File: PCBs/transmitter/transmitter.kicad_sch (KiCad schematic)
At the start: 20 parts, among them J1 Conn_01x02, J11 LoRa, J2 GPIO, J3 Ethernet, J4 Thermistor (10K), J5 RF24, J6 SWD, J7 I2C, J8 Serial, SW1 ~{RESET}

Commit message: created fabrication outputs
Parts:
- H1: footprint (none) -> MountingHole:MountingHole_2mm
- J11, J3: footprint Connector_PinSocket_2.54mm:PinSocket_1x08_P2.54mm_Vertical -> Connector_PinHeader_2.54mm:PinHeader_1x08_P2.54mm_Vertical
- J2, J6, J7, J8: footprint Connector_PinSocket_2.54mm:PinSocket_1x04_P2.54mm_Vertical -> Connector_PinHeader_2.54mm:PinHeader_1x04_P2.54mm_Vertical
- J5: footprint Connector_PinSocket_2.54mm:PinSocket_1x07_P2.54mm_Vertical -> Connector_PinHeader_2.54mm:PinHeader_1x07_P2.54mm_Vertical
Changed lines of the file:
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@@
     (property "Reference" "J11" (id 0) (at 254 92.71 0))
     (property "Value" "LoRa" (id 1) (at 254 95.25 0))
-    (property "Footprint" "Connector_PinSocket_2.54mm:PinSocket_1x08_P2.54mm_Vertical" (id 2) (at 254 109.22 0)
+    (property "Footprint" "Connector_PinHeader_2.54mm:PinHeader_1x08_P2.54mm_Vertical" (id 2) (at 254 109.22 0)
       (effects (font (size 1.27 1.27)) hide)
     )
@@
     (property "Reference" "J3" (id 0) (at 207.01 31.75 0))
     (property "Value" "Ethernet" (id 1) (at 207.01 34.29 0))
-    (property "Footprint" "Connector_PinSocket_2.54mm:PinSocket_1x08_P2.54mm_Vertical" (id 2) (at 207.01 48.26 0)
+    (property "Footprint" "Connector_PinHeader_2.54mm:PinHeader_1x08_P2.54mm_Vertical" (id 2) (at 207.01 48.26 0)
       (effects (font (size 1.27 1.27)) hide)
     )
@@
     (property "Reference" "J5" (id 0) (at 231.14 36.83 0))
     (property "Value" "RF24" (id 1) (at 231.14 39.37 0))
-    (property "Footprint" "Connector_PinSocket_2.54mm:PinSocket_1x07_P2.54mm_Vertical" (id 2) (at 231.14 50.8 0)
+    (property "Footprint" "Connector_PinHeader_2.54mm:PinHeader_1x07_P2.54mm_Vertical" (id 2) (at 231.14 50.8 0)
       (effects (font (size 1.27 1.27)) hide)
     )
@@
     (property "Reference" "J7" (id 0) (at 256.54 40.64 0))
     (property "Value" "I2C" (id 1) (at 256.54 43.18 0))
-    (property "Footprint" "Connector_PinSocket_2.54mm:PinSocket_1x04_P2.54mm_Vertical" (id 2) (at 256.54 52.07 0)
+    (property "Footprint" "Connector_PinHeader_2.54mm:PinHeader_1x04_P2.54mm_Vertical" (id 2) (at 256.54 52.07 0)
       (effects (font (size 1.27 1.27)) hide)
     )
@@
     (property "Reference" "J8" (id 0) (at 257.81 67.31 0))
     (property "Value" "Serial" (id 1) (at 257.81 69.85 0))
-    (property "Footprint" "Connector_PinSocket_2.54mm:PinSocket_1x04_P2.54mm_Vertical" (id 2) (at 257.81 78.74 0)
+    (property "Footprint" "Connector_PinHeader_2.54mm:PinHeader_1x04_P2.54mm_Vertical" (id 2) (at 257.81 78.74 0)
       (effects (font (size 1.27 1.27)) hide)
     )
@@
     (property "Reference" "J6" (id 0) (at 234.95 67.31 0))
     (property "Value" "SWD" (id 1) (at 234.95 69.85 0))
-    (property "Footprint" "Connector_PinSocket_2.54mm:PinSocket_1x04_P2.54mm_Vertical" (id 2) (at 234.95 78.74 0)
+    (property "Footprint" "Connector_PinHeader_2.54mm:PinHeader_1x04_P2.54mm_Vertical" (id 2) (at 234.95 78.74 0)
       (effects (font (size 1.27 1.27)) hide)
     )
@@
     (property "Reference" "J2" (id 0) (at 190.5 62.23 0))
     (property "Value" "GPIO" (id 1) (at 190.5 64.77 0))
-    (property "Footprint" "Connector_PinSocket_2.54mm:PinSocket_1x04_P2.54mm_Vertical" (id 2) (at 190.5 73.66 0)
+    (property "Footprint" "Connector_PinHeader_2.54mm:PinHeader_1x04_P2.54mm_Vertical" (id 2) (at 190.5 73.66 0)
       (effects (font (size 1.27 1.27)) hide)
     )
@@
       (effects (font (size 1.27 1.27)) (justify left))
     )
-    (property "Footprint" "" (id 2) (at 35.56 179.07 0)
+    (property "Footprint" "MountingHole:MountingHole_2mm" (id 2) (at 35.56 179.07 0)
       (effects (font (size 1.27 1.27)) hide)
     )
@@
     )
     (path "/b6492f65-6790-4444-8f40-ae63444e55da"
-      (reference "J2") (unit 1) (value "GPIO") (footprint "Connector_PinSocket_2.54mm:PinSocket_1x04_P2.54mm_Vertical")
+      (reference "J2") (unit 1) (value "GPIO") (footprint "Connector_PinHeader_2.54mm:PinHeader_1x04_P2.54mm_Vertical")
     )
     (path "/148e4b07-2754-41fa-b362-f32ae5e0b598"
-      (reference "J3") (unit 1) (value "Ethernet") (footprint "Connector_PinSocket_2.54mm:PinSocket_1x08_P2.54mm_Vertical")
+      (reference "J3") (unit 1) (value "Ethernet") (footprint "Connector_PinHeader_2.54mm:PinHeader_1x08_P2.54mm_Vertical")
     )
     (path "/fd4589a9-f46c-4fce-a160-6787f4809f25"
@@
     )
     (path "/23618512-a2f8-44e6-8cd2-358294831b6f"
-      (reference "J5") (unit 1) (value "RF24") (footprint "Connector_PinSocket_2.54mm:PinSocket_1x07_P2.54mm_Vertical")
+      (reference "J5") (unit 1) (value "RF24") (footprint "Connector_PinHeader_2.54mm:PinHeader_1x07_P2.54mm_Vertical")
     )
     (path "/9c0e092b-e2d2-4772-898a-4fdfc0c9fe18"
-      (reference "J6") (unit 1) (value "SWD") (footprint "Connector_PinSocket_2.54mm:PinSocket_1x04_P2.54mm_Vertical")
+      (reference "J6") (unit 1) (value "SWD") (footprint "Connector_PinHeader_2.54mm:PinHeader_1x04_P2.54mm_Vertical")
     )
     (path "/3d3b00a9-2614-4561-9134-a45b0c6831cd"
-      (reference "J7") (unit 1) (value "I2C") (footprint "Connector_PinSocket_2.54mm:PinSocket_1x04_P2.54mm_Vertical")
+      (reference "J7") (unit 1) (value "I2C") (footprint "Connector_PinHeader_2.54mm:PinHeader_1x04_P2.54mm_Vertical")
     )
     (path "/4caa9778-cadd-482a-8556-4989310bc954"
-      (reference "J8") (unit 1) (value "Serial") (footprint "Connector_PinSocket_2.54mm:PinSocket_1x04_P2.54mm_Vertical")
+      (reference "J8") (unit 1) (value "Serial") (footprint "Connector_PinHeader_2.54mm:PinHeader_1x04_P2.54mm_Vertical")
     )
     (path "/d7224ebd-0e44-4d03-8a13-9628956cf16f/199f531d-1d56-48d3-bbb1-c98ffceed090"
@@
     )
     (path "/0e660b53-fd61-484a-b5ba-116ad7753a8a"
-      (reference "J11") (unit 1) (value "LoRa") (footprint "Connector_PinSocket_2.54mm:PinSocket_1x08_P2.54mm_Vertical")
+      (reference "J11") (unit 1) (value "LoRa") (footprint "Connector_PinHeader_2.54mm:PinHeader_1x08_P2.54mm_Vertical")
     )
     (path "/165f464f-66cd-43f3-872c-58af3ebdb812/198b5ba2-3238-4b90-8afe-766f8c4b230b"

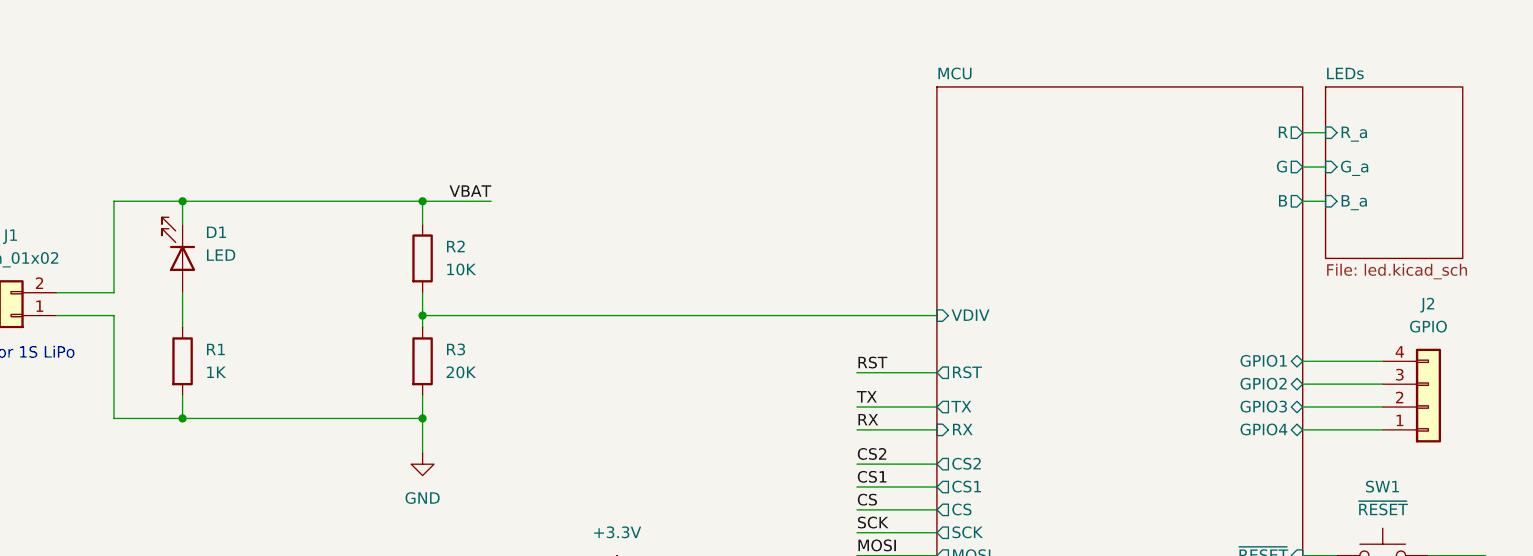
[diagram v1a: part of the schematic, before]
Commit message: created sensor board
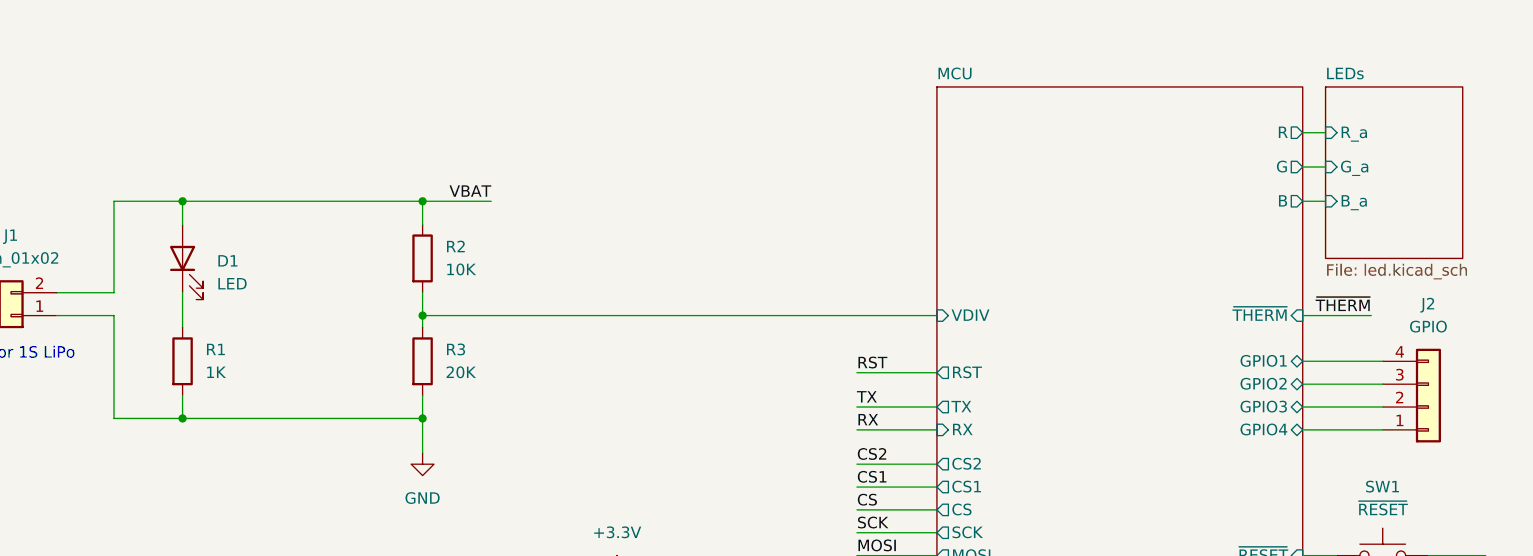
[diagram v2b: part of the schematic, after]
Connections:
- net VBAT: now also D1.2 (A); no longer D1.1 (K)
- net at R1.1: now also D1.1 (K); no longer D1.2 (A)
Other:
- sheet MCU ports: added ~{THERM}; removed none
- moved on the sheet: D1
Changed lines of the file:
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@@
+    (stroke (width 0) (type default) (color 0 0 0 0))
+  )
+  (wire (pts (xy 176.53 63.5) (xy 184.15 63.5))
     (stroke (width 0) (type default) (color 0 0 0 0))
   )
@@
   )
   (label "CHG" (at 186.69 95.25 180)
+    (effects (font (size 1.27 1.27)) (justify right bottom))
+  )
+  (label "~{THERM}" (at 184.15 63.5 180)
     (effects (font (size 1.27 1.27)) (justify right bottom))
   )
@@
     (pin "2")
   )
-  (symbol (lib_id "Device:LED") (at 52.07 57.15 270) (unit 1)
-    (in_bom yes) (on_board yes) (fields_autoplaced)
-    (property "Reference" "D1" (id 0) (at 54.61 54.2924 90)
-      (effects (font (size 1.27 1.27)) (justify left))
-    )
-    (property "Value" "LED" (id 1) (at 54.61 56.8324 90)
-      (effects (font (size 1.27 1.27)) (justify left))
+  (symbol (lib_id "Device:LED") (at 52.07 57.15 90) (unit 1)
+    (in_bom yes) (on_board yes) (fields_autoplaced)
+    (property "Reference" "D1" (id 0) (at 55.88 57.4674 90)
+      (effects (font (size 1.27 1.27)) (justify right))
+    )
+    (property "Value" "LED" (id 1) (at 55.88 60.0074 90)
+      (effects (font (size 1.27 1.27)) (justify right))
     )
     (property "Footprint" "LED_SMD:LED_0603_1608Metric" (id 2) (at 52.07 57.15 0)
@@
       (effects (font (size 1.27 1.27)) (justify left))
     )
-  )
+    (pin "~{THERM}" input (at 176.53 63.5 0)
+      (effects (font (size 1.27 1.27)) (justify right))
+    )
+  )
